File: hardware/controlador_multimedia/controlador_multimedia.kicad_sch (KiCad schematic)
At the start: 19 parts, among them J1 Conn_01x15, J2 Conn_01x15, J3 Conn_01x06, J4 Conn_01x06, J5 Conn_01x04, J6 Conn_01x04, J7 Conn_01x03, J8 Conn_01x02, SW1 SW_Push, SW2 SW_Push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

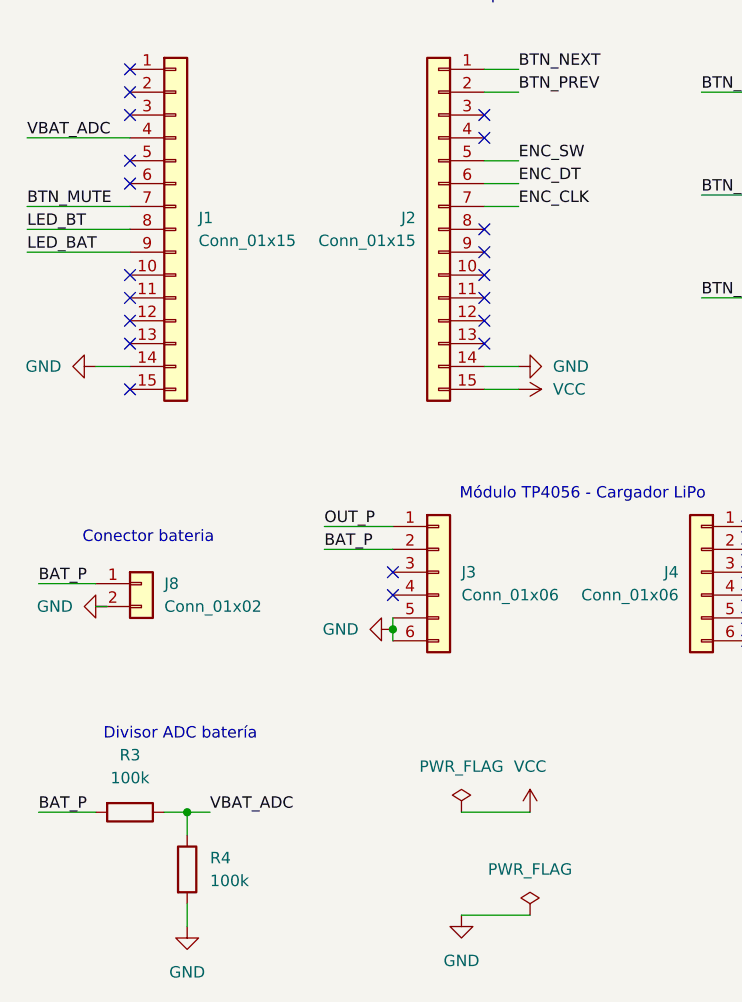
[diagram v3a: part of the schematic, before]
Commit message: hardware: agregar diseño PCB v1.0 con ruteo completo, plano GND y Gerbers
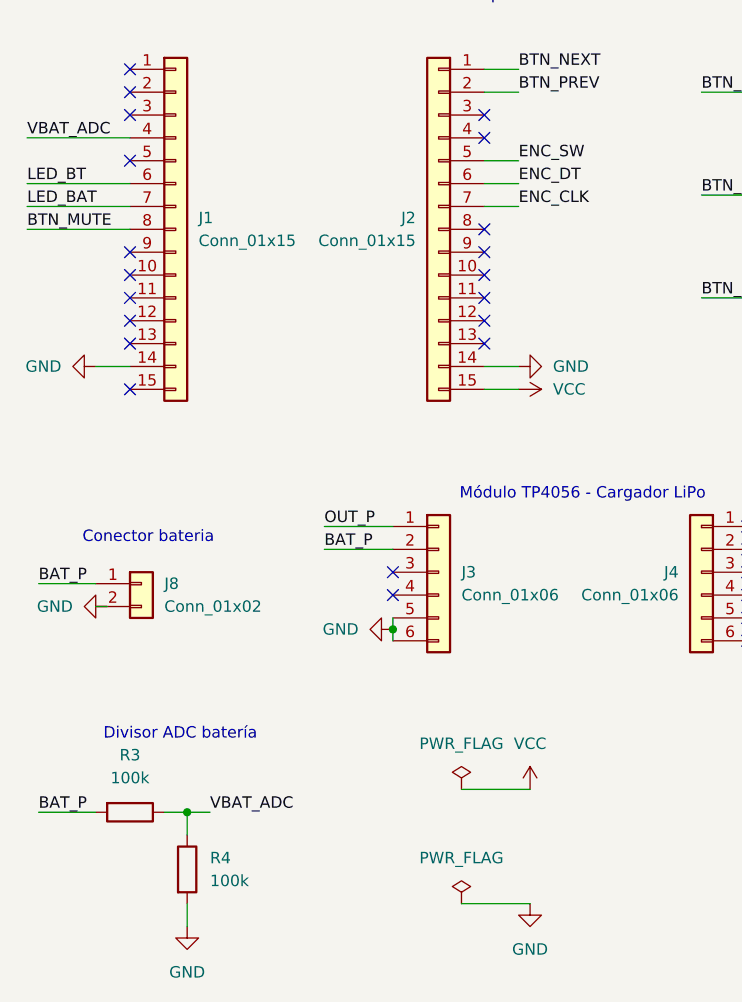
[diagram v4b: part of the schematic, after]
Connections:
- net BTN_MUTE: now also J1.8 (Pin_8); no longer J1.7 (Pin_7)
- net LED_BAT: now also J1.7 (Pin_7); no longer J1.9 (Pin_9)
- net LED_BT: now also J1.6 (Pin_6); no longer J1.8 (Pin_8)
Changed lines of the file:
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@@
+	)
+	(no_connect
+		(at 29.21 38.1)
 	)
 	(no_connect
@@
 	)
 	(no_connect
-		(at 29.21 40.64)
-	)
-	(no_connect
 		(at 68.58 53.34)
 	)
@@
 	)
 	(no_connect
+		(at 29.21 48.26)
+	)
+	(no_connect
 		(at 29.21 58.42)
 	)
@@
 	)
 	(no_connect
-		(at 29.21 38.1)
-	)
-	(no_connect
 		(at 119.38 85.09)
 	)
@@
 	(wire
 		(pts
-			(xy 66.04 121.92) (xy 73.66 121.92)
-		)
-		(stroke
-			(width 0)
-			(type default)
-		)
-	)
-	(wire
-		(pts
 			(xy 143.51 44.45) (xy 146.05 44.45)
 		)
@@
 	(wire
 		(pts
-			(xy 66.04 110.49) (xy 73.66 110.49)
+			(xy 66.04 107.95) (xy 73.66 107.95)
 		)
 		(stroke
@@
 	(wire
 		(pts
+			(xy 156.21 27.94) (xy 165.1 27.94)
+		)
+		(stroke
+			(width 0)
+			(type default)
+		)
+	)
+	(wire
+		(pts
 			(xy 17.78 43.18) (xy 29.21 43.18)
 		)
@@
 	(wire
 		(pts
-			(xy 156.21 27.94) (xy 165.1 27.94)
-		)
-		(stroke
-			(width 0)
-			(type default)
-		)
-	)
-	(wire
-		(pts
 			(xy 35.56 110.49) (xy 35.56 113.03)
 		)
@@
 	(wire
 		(pts
+			(xy 17.78 45.72) (xy 29.21 45.72)
+		)
+		(stroke
+			(width 0)
+			(type default)
+		)
+	)
+	(wire
+		(pts
 			(xy 181.61 80.01) (xy 184.15 80.01)
 		)
@@
 	(wire
 		(pts
-			(xy 17.78 48.26) (xy 29.21 48.26)
-		)
-		(stroke
-			(width 0)
-			(type default)
-		)
-	)
-	(wire
-		(pts
 			(xy 177.8 27.94) (xy 177.8 29.21)
 		)
@@
 	(wire
 		(pts
+			(xy 73.66 120.65) (xy 66.04 120.65)
+		)
+		(stroke
+			(width 0)
+			(type default)
+		)
+	)
+	(wire
+		(pts
 			(xy 118.11 44.45) (xy 128.27 44.45)
 		)
@@
 	(wire
 		(pts
+			(xy 17.78 40.64) (xy 29.21 40.64)
+		)
+		(stroke
+			(width 0)
+			(type default)
+		)
+	)
+	(wire
+		(pts
 			(xy 140.97 80.01) (xy 142.24 80.01)
 		)
@@
 		(pts
 			(xy 165.1 27.94) (xy 165.1 29.21)
-		)
-		(stroke
-			(width 0)
-			(type default)
-		)
-	)
-	(wire
-		(pts
-			(xy 17.78 45.72) (xy 29.21 45.72)
 		)
 		(stroke
@@
 	)
 	(label "LED_BT"
-		(at 17.78 45.72 0)
+		(at 17.78 40.64 0)
 		(effects
 			(font
@@
 	)
 	(label "BTN_MUTE"
-		(at 17.78 43.18 0)
+		(at 17.78 45.72 0)
 		(effects
 			(font
@@
 	)
 	(label "LED_BAT"
-		(at 17.78 48.26 0)
+		(at 17.78 43.18 0)
 		(effects
 			(font
@@
 	(symbol
 		(lib_id "power:PWR_FLAG")
-		(at 73.66 121.92 0)
+		(at 66.04 120.65 0)
 		(unit 1)
 		(exclude_from_sim no)
@@
 		(fields_autoplaced yes)
 		(property "Reference" "#FLG2"
-			(at 73.66 120.015 0)
+			(at 66.04 118.745 0)
 			(effects
 				(font
@@
 		)
 		(property "Value" "PWR_FLAG"
-			(at 73.66 116.84 0)
+			(at 66.04 115.57 0)
 			(effects
 				(font
@@
 		)
 		(property "Footprint" ""
-			(at 73.66 121.92 0)
+			(at 66.04 120.65 0)
 			(effects
 				(font
@@
 		)
 		(property "Datasheet" "~"
-			(at 73.66 121.92 0)
+			(at 66.04 120.65 0)
 			(effects
 				(font
@@
 		)
 		(property "Description" "Special symbol for telling ERC where power comes from"
-			(at 73.66 121.92 0)
+			(at 66.04 120.65 0)
 			(effects
 				(font
@@
 	(symbol
 		(lib_id "power:GND")
-		(at 66.04 121.92 0)
+		(at 73.66 120.65 0)
 		(unit 1)
 		(exclude_from_sim no)
@@
 		(fields_autoplaced yes)
 		(property "Reference" "#PWR10"
-			(at 66.04 128.27 0)
+			(at 73.66 127 0)
 			(effects
 				(font
@@
 		)
 		(property "Value" "GND"
-			(at 66.04 127 0)
+			(at 73.66 125.73 0)
 			(effects
 				(font
@@
 		)
 		(property "Footprint" ""
-			(at 66.04 121.92 0)
+			(at 73.66 120.65 0)
 			(effects
 				(font
@@
 		)
 		(property "Datasheet" ""
-			(at 66.04 121.92 0)
+			(at 73.66 120.65 0)
 			(effects
 				(font
@@
 		)
 		(property "Description" "Power symbol creates a global label with name \"GND\" , ground"
-			(at 66.04 121.92 0)
+			(at 73.66 120.65 0)
 			(effects
 				(font
@@
 	(symbol
 		(lib_id "power:PWR_FLAG")
-		(at 66.04 110.49 0)
+		(at 66.04 107.95 0)
 		(unit 1)
 		(exclude_from_sim no)
@@
 		(fields_autoplaced yes)
 		(property "Reference" "#FLG1"
-			(at 66.04 108.585 0)
+			(at 66.04 106.045 0)
 			(effects
 				(font
@@
 		)
 		(property "Value" "PWR_FLAG"
-			(at 66.04 105.41 0)
+			(at 66.04 102.87 0)
 			(effects
 				(font
@@
 		)
 		(property "Footprint" ""
-			(at 66.04 110.49 0)
+			(at 66.04 107.95 0)
 			(effects
 				(font
@@
 		)
 		(property "Datasheet" "~"
-			(at 66.04 110.49 0)
+			(at 66.04 107.95 0)
 			(effects
 				(font
@@
 		)
 		(property "Description" "Special symbol for telling ERC where power comes from"
-			(at 66.04 110.49 0)
+			(at 66.04 107.95 0)
 			(effects
 				(font
@@
 	(symbol
 		(lib_id "power:VCC")
-		(at 73.66 110.49 0)
+		(at 73.66 107.95 0)
 		(unit 1)
 		(exclude_from_sim no)
@@
 		(fields_autoplaced yes)
 		(property "Reference" "#PWR11"
-			(at 73.66 114.3 0)
+			(at 73.66 111.76 0)
 			(effects
 				(font
@@
 		)
 		(property "Value" "VCC"
-			(at 73.66 105.41 0)
+			(at 73.66 102.87 0)
 			(effects
 				(font
@@
 		)
 		(property "Footprint" ""
-			(at 73.66 110.49 0)
+			(at 73.66 107.95 0)
 			(effects
 				(font
@@
 		)
 		(property "Datasheet" ""
-			(at 73.66 110.49 0)
+			(at 73.66 107.95 0)
 			(effects
 				(font
@@
 		)
 		(property "Description" "Power symbol creates a global label with name \"VCC\""
-			(at 73.66 110.49 0)
-			(effects
-				(font
+			(at 73.66 107.95 0)
+			(effects
+				(font
